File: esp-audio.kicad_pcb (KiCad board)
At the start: 2 copper layers, 43.2 x 73.7 mm, 75 parts, among them J1 PJ-342B, J2 HR911105A, J3 USB_C_Receptacle_USB2.0, J4 Conn_01x03_Socket, J5 Conn_01x12_Pin, SW1 SW_Push, SW2 SW_Push, U1 W5500, U10 MT2492, U2 ESP32-S3-WROOM-1U-N8R8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

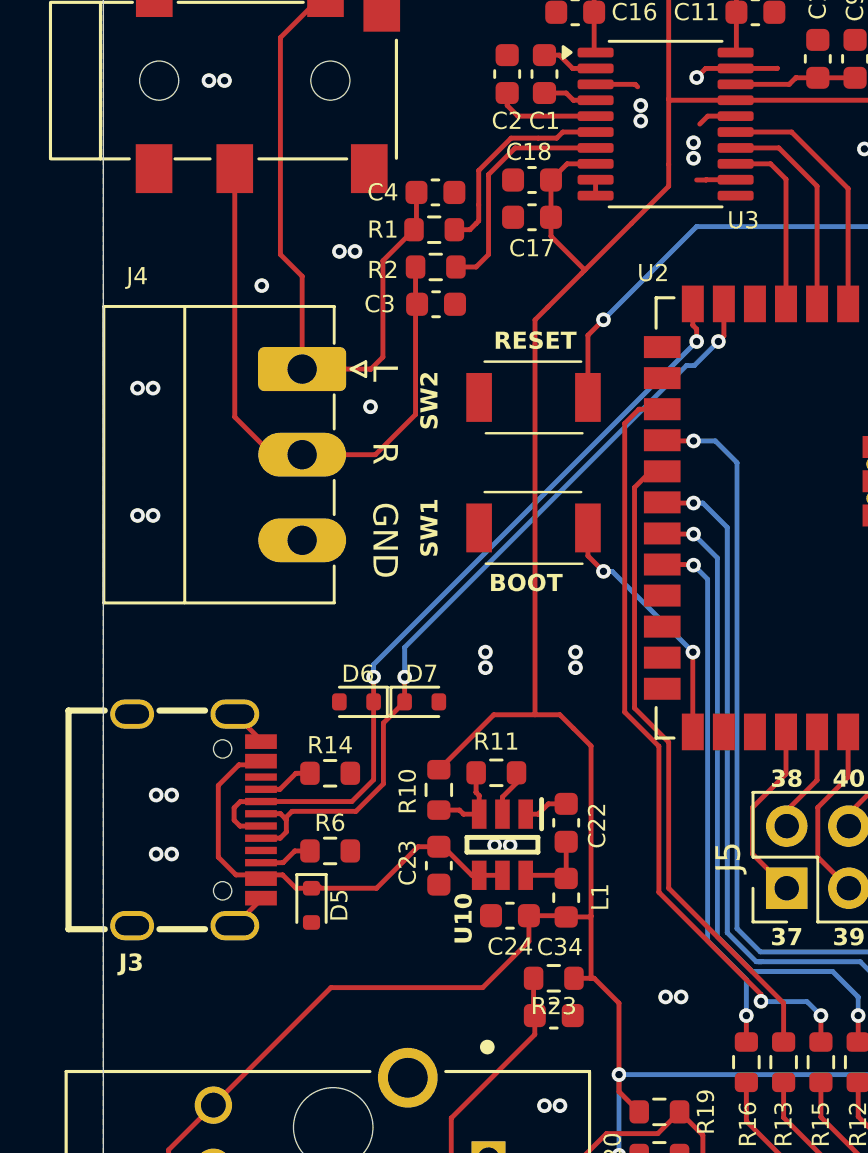
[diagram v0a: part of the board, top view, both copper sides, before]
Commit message: fix USB D+/D-, caps, add power pins
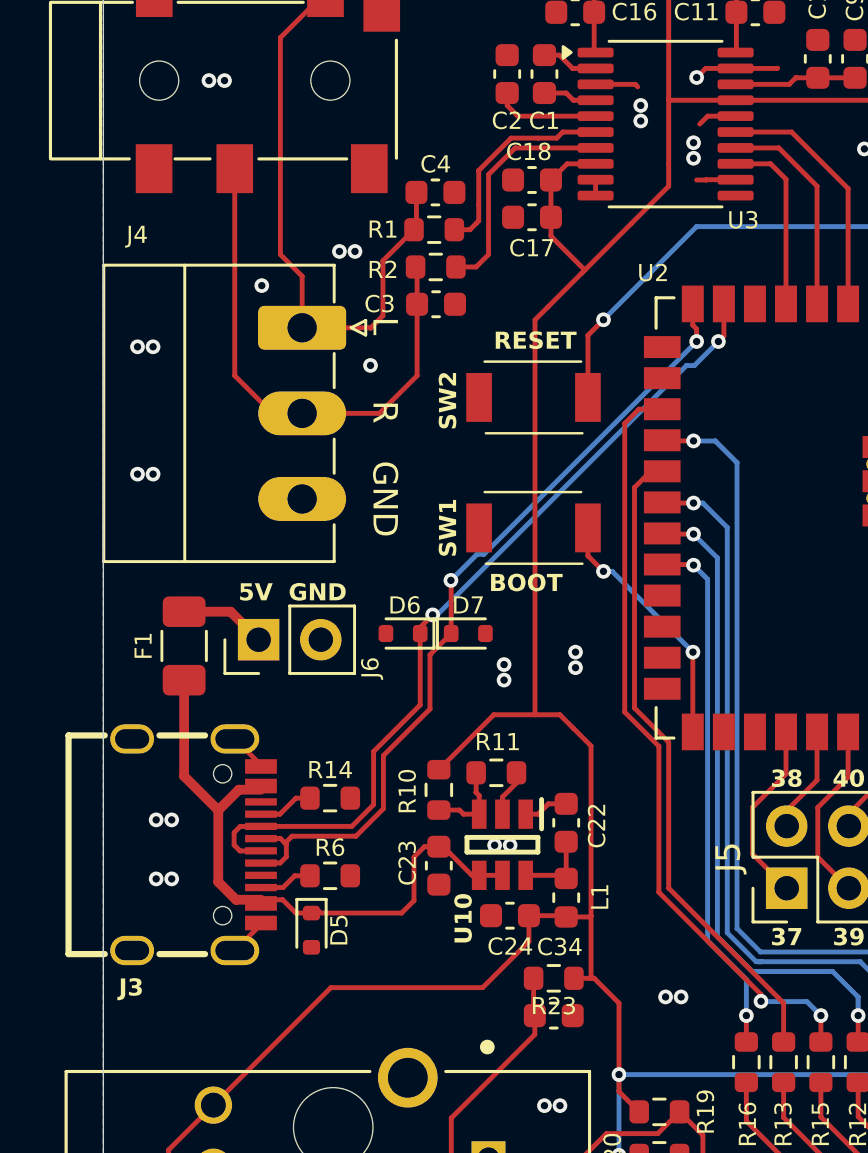
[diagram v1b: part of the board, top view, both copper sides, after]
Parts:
- added F1: 3A 12V, Fuse:Fuse_1206_3216Metric, F.Cu at (140.5, 91.7)
- added J6: Conn_01x02_Pin, Connector_PinHeader_2.54mm:PinHeader_1x02_P2.54mm_Vertical, F.Cu at (143.5, 91.4)
- C3, C4: value 2.2uF -> 2.2nF
- moved D6 3.38 mm to (149.4, 91.2)
- moved D7 3.38 mm to (152.1, 91.2)
- moved J4 1.69 mm to (145.3, 78.7)
- moved D5 1.02 mm to (145.7, 103.3)
- moved J3 1.02 mm to (141.0, 99.8)
- moved R14 1.02 mm to (146.4, 97.9)
- moved R6 1.02 mm to (146.4, 101.1)
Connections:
- D6 pad 1: /D+ -> /D-
- D7 pad 1: /D- -> /D+
- J3 pad A6: /D- -> /D+
- J3 pad A7: /D+ -> /D-
- J3 pad B6: /D- -> /D+
- J3 pad B7: /D+ -> /D-
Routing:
- net VBUS: track 18.7 -> 26.1 mm
- net Net-(J6-Pin_1): track 0.00 -> 3.52 mm
- net /OUTL: track 27.3 -> 24.0 mm
- net /OUTR: track 24.9 -> 21.7 mm
- net /D-: track 33.7 -> 35.1 mm
- net /D+: track 32.9 -> 33.7 mm
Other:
- board text added: "5V"

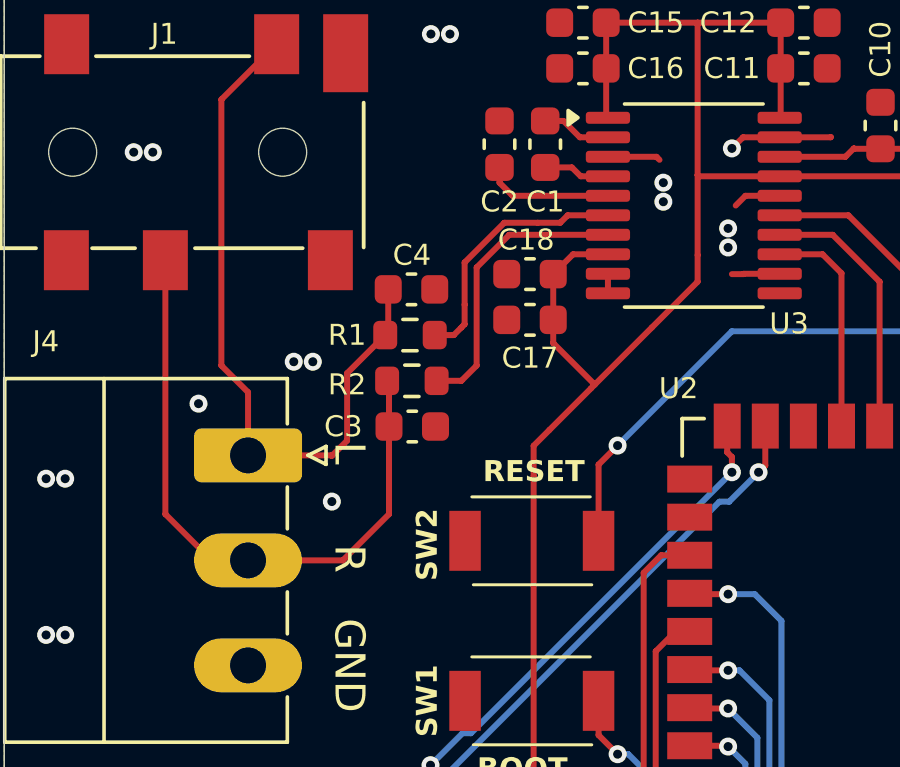
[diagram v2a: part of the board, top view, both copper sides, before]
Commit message: added mono mix pin header (jumper pins to mix L and R channels)
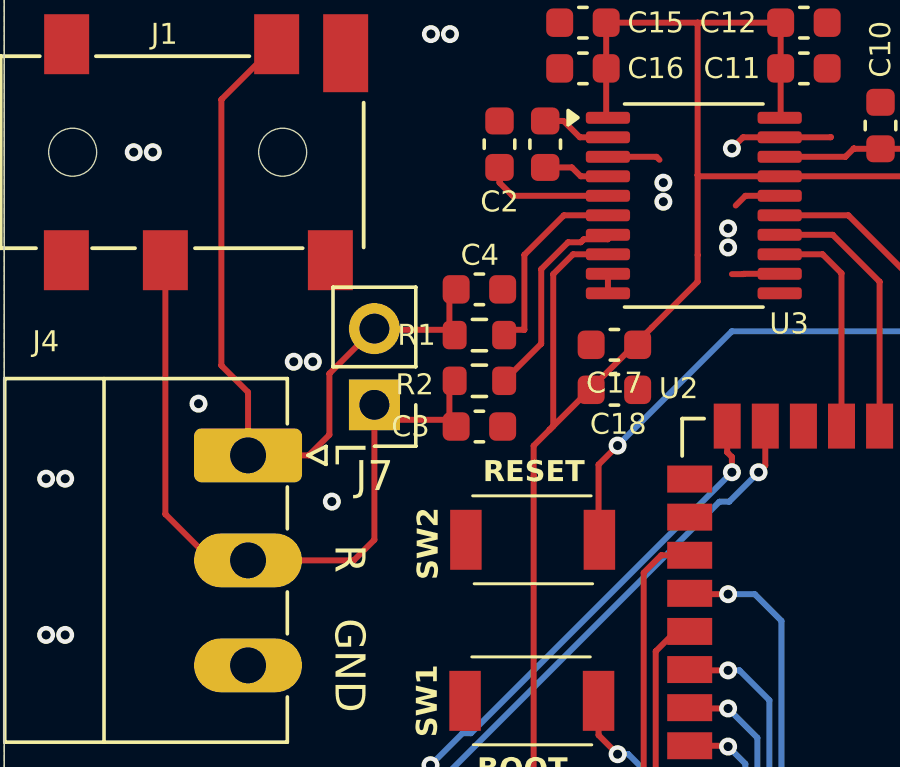
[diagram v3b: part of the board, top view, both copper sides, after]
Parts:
- added J7: <= MONO_MIX, Connector_PinHeader_2.54mm:PinHeader_1x02_P2.54mm_Vertical, F.Cu at (149.5, 77.0)
- moved C18 4.77 mm to (157.5, 76.5), turned to 0 degrees
- moved C17 2.93 mm to (157.5, 75.0)
- moved R1 2.31 mm to (153.0, 74.7)
- moved C4 2.26 mm to (153.0, 73.2)
- moved R2 2.25 mm to (153.0, 76.2)
- moved C3 2.24 mm to (153.0, 77.7)
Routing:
- net Net-(U3-OUTL): track 8.63 -> 3.33 mm
- net Net-(U3-OUTR): track 9.64 -> 7.02 mm
- net /OUTL: track 24.0 -> 22.0 mm
- net +3V3: track 200.5 -> 201.5 mm
- net /OUTR: track 21.7 -> 20.9 mm
